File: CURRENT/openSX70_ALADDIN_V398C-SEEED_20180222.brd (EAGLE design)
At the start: 95.9 x 27.9 mm, 45 parts, among them Q1 5.8A/30V/35mΩ, Q2 5.8A/30V/35mΩ, U1 ATMEGA328P_TQFP, U3 BH1750FVI-TR, Y1 CSTCE8M00G52Z-R0

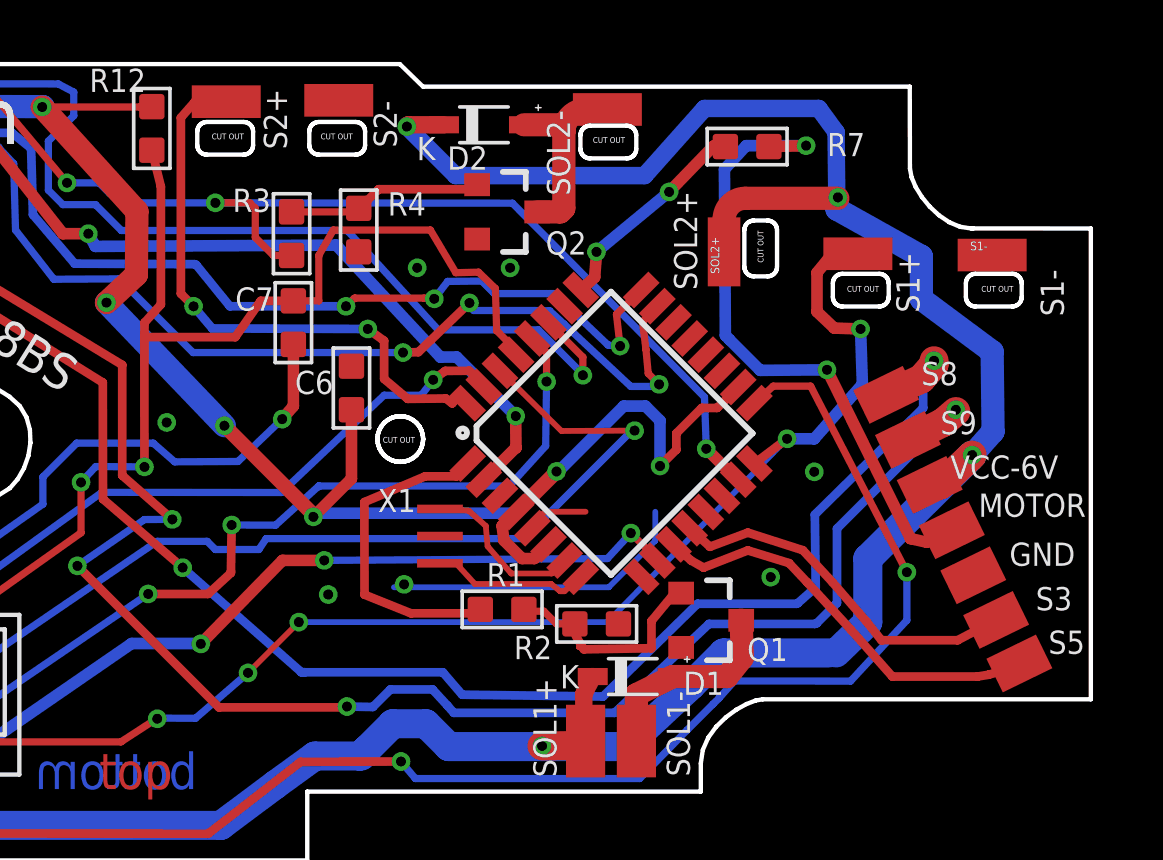
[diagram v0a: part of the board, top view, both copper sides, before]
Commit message: New board nickname: Len's&Bellows 5.0 (different from Len's & Bellows 4.x): moved Atmega up, and much more little improvements!
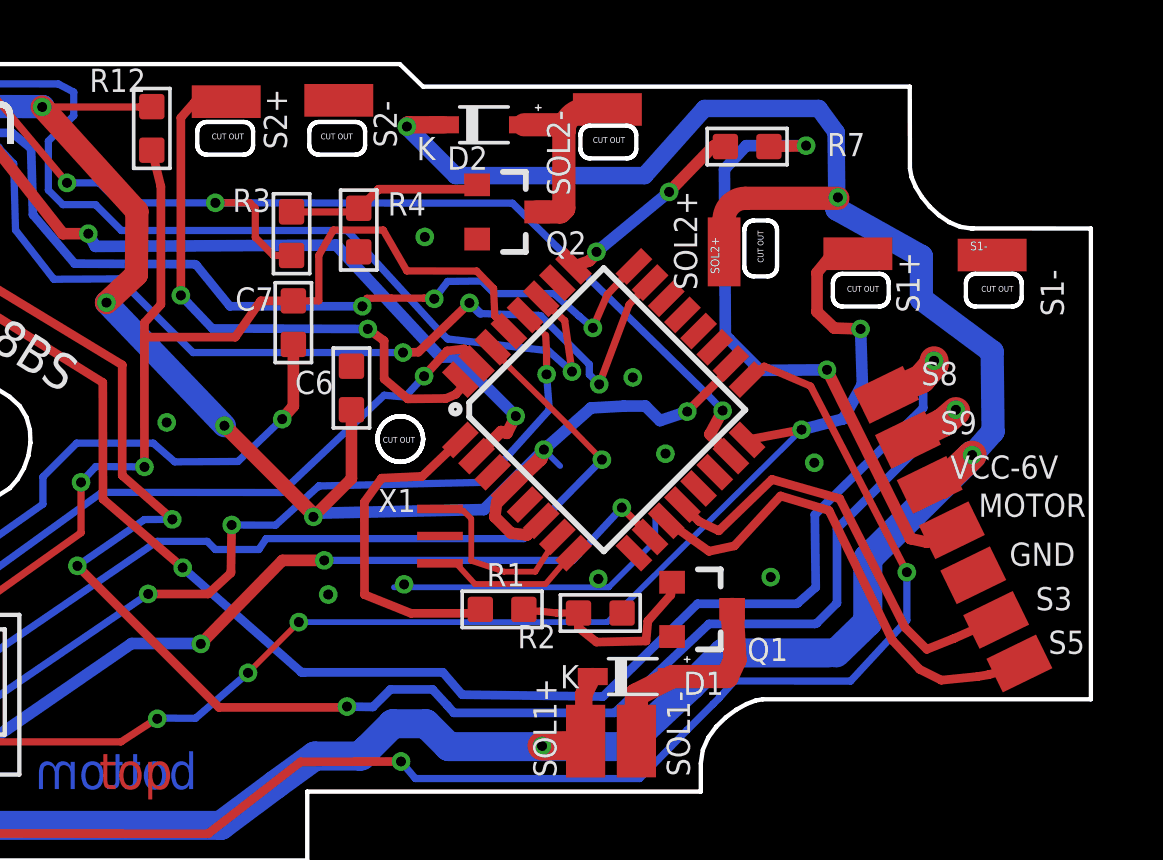
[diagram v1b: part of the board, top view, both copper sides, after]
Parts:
- moved U1 0.86 mm to (80.9, 16.6)
- moved Q1 0.50 mm to (84.3, 9.59)
- moved R2 0.40 mm to (80.8, 9.46)
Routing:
- net S3: track 12.8 -> 15.4 mm
- net S5: track 15.3 -> 17.9 mm
- net GND: track 15.5 -> 12.9 mm, vias 11 -> 13
- net 3.3V: track 156.5 -> 154.4 mm
- net 100R: track 109.2 -> 107.6 mm
- net S9@2.5V: track 77.1 -> 76.0 mm
- net N$1: track 8.35 -> 7.36 mm
- net S8@2.5V: track 69.1 -> 68.2 mm
- net FF: track 70.3 -> 69.7 mm
- net SOL2: track 90.5 -> 89.9 mm
- net N$4: track 6.09 -> 6.67 mm
- net MOTOR+: track 7.49 -> 6.95 mm
